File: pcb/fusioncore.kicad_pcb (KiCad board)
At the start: 2 copper layers, 95 x 99 mm, 116 parts, among them J1 Conn_02x12_Top_Bottom, J10 Pump_Misc_1, J11 Pump_Misc_2, J12 Flow_Warm, J13 Flow_Cold, J14 Trigger, J15 Valve_M2, J16 Valve_M3, J17 Valve_M4, J18 Conn_02x03_Top_Bottom, J19 Valve_Air_Lime, J2 Temperature, J20 Valve_Air_Rum, J21 Valve_Air_Out, J22 LED, J23 I2C_DBG, J3 40HAT, J4 Valve_M1, J5 WEIGHT, J6 Pump_Cold, J7 Pump_Warm, J8 Pump_Air, J9 CONN_01X02, Q1 DMG2305UX, Q12 AO3400A, Q13 AO3400A, Q14 AO3400A, Q16 MMBT4403, Q2 DMMT5401, Q3 AO3400A, Q4 AO3400A, Q5 AO3400A, Q6 AO3400A, Q7 AO3400A, SW1 POWER_ON, U1 HX711, U2 CAT24C32, U3 LTC2990, U4 LTC2990, U5 TXB0108DQSR

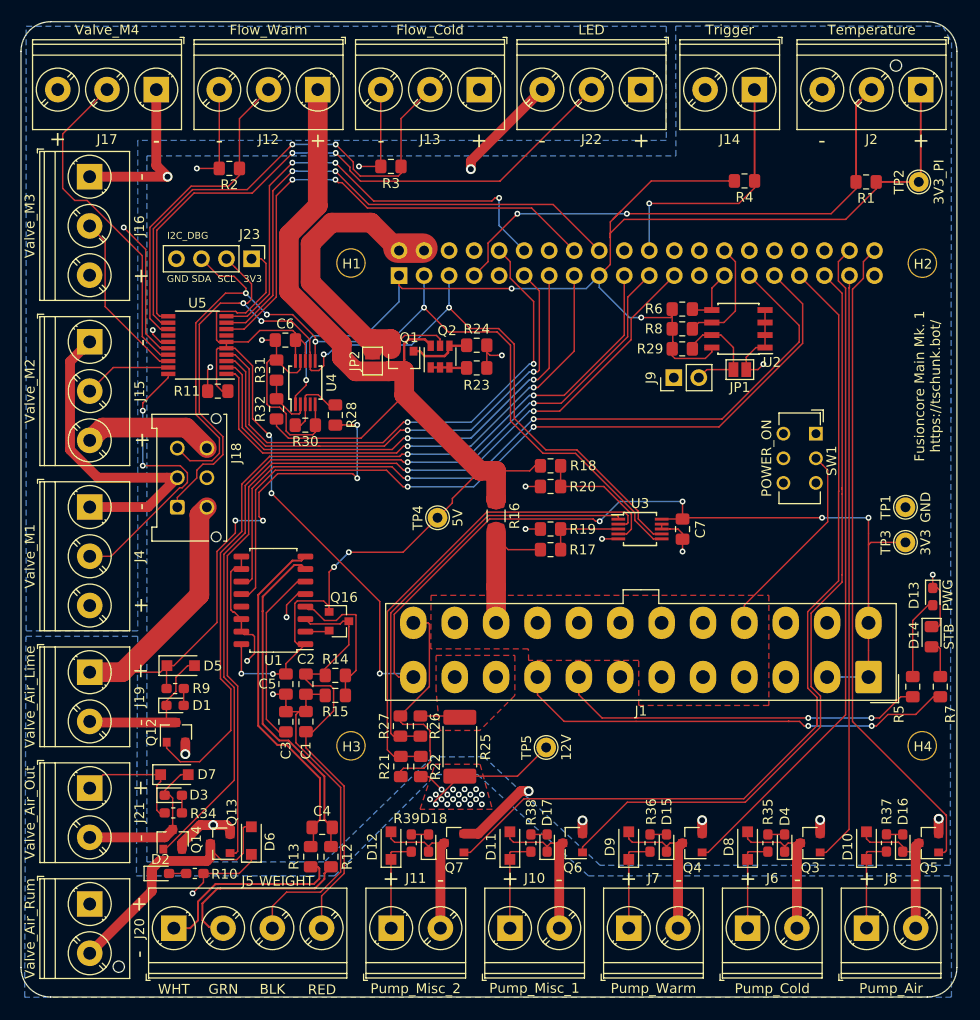
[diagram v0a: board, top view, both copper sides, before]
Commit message: Replaced LTC2990 with INA226 on pcb layout as well
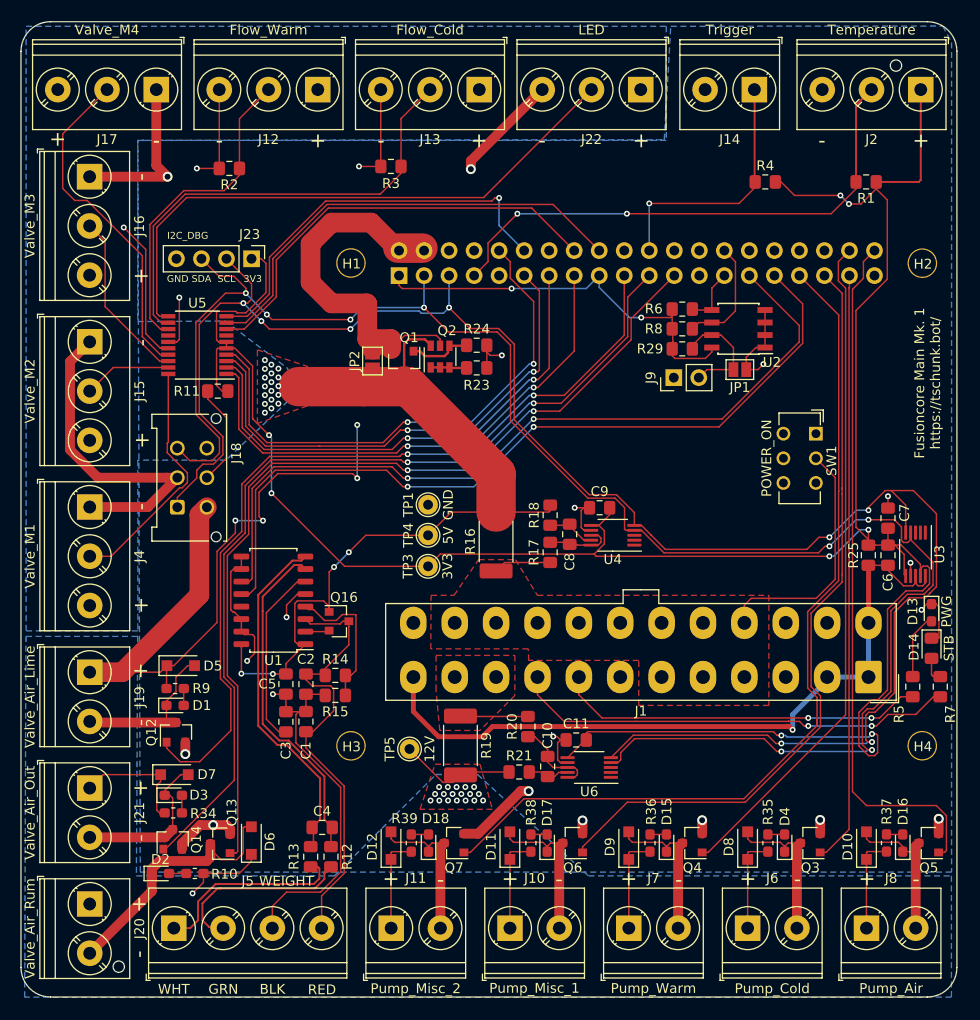
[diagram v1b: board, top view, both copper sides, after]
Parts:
- removed R22, R26, R28, R32: 100K, Resistor_SMD:R_0805_2012Metric_Pad1.15x1.40mm_HandSolder
- removed R27, R30: 20K, Resistor_SMD:R_0805_2012Metric_Pad1.15x1.40mm_HandSolder
- removed R31: 47K, Resistor_SMD:R_0805_2012Metric_Pad1.15x1.40mm_HandSolder
- removed TP2: 3V3_PI, TestPoint:TestPoint_THTPad_D2.0mm_Drill1.0mm
- added C10: 0.1μF, Capacitor_SMD:C_0805_2012Metric_Pad1.15x1.40mm_HandSolder, F.Cu at (102.0, 115.4)
- added C11: 0.1μF, Capacitor_SMD:C_0805_2012Metric_Pad1.15x1.40mm_HandSolder, F.Cu at (104.9, 112.7)
- added C8: 0.1μF, Capacitor_SMD:C_0805_2012Metric_Pad1.15x1.40mm_HandSolder, F.Cu at (104.2, 91.8)
- added C9: 0.1μF, Capacitor_SMD:C_0805_2012Metric_Pad1.15x1.40mm_HandSolder, F.Cu at (107.3, 89.2)
- added U6: INA226, Package_SO:VSSOP-10_3x3mm_P0.5mm, F.Cu at (106.2, 115.5)
- R16: value 0.15 -> 0.008; footprint Resistor_SMD:R_1206_3216Metric_Pad1.42x1.75mm_HandSolder -> Resistor_SMD:R_2512_6332Metric_Pad1.52x3.35mm_HandSolder
- R17, R18: value 100K -> 10
- R19: value 47K -> 0.008; footprint Resistor_SMD:R_0805_2012Metric_Pad1.15x1.40mm_HandSolder -> Resistor_SMD:R_2512_6332Metric_Pad1.52x3.35mm_HandSolder
- R20: value 47K -> 10
- R21: value 20K -> 10
- R25: footprint Resistor_SMD:R_2512_6332Metric_Pad1.52x3.35mm_HandSolder -> Resistor_SMD:R_0805_2012Metric_Pad1.15x1.40mm_HandSolder
- U3, U4: value LTC2990 -> INA226; footprint Package_SO:MSOP-10_3x3mm_P0.5mm -> Package_SO:VSSOP-10_3x3mm_P0.5mm
- moved C6 64.9 mm to (136.6, 94.0), turned to 270 degrees
- moved TP3 48.5 mm to (89.9, 95.1), turned to 270 degrees
- moved TP1 48.5 mm to (89.9, 88.8)
- moved R25 45.8 mm to (134.6, 94.0), turned to 90 degrees
- moved U4 34.8 mm to (108.6, 91.9), turned to 180 degrees
- moved U3 28.1 mm to (139.3, 93.9), turned to 270 degrees
- moved R20 24.5 mm to (100.0, 111.4), turned to 270 degrees
- moved R19 23.8 mm to (93.2, 113.3), turned to 270 degrees
- moved C7 20.9 mm to (136.6, 90.2), turned to 270 degrees
- moved TP5 13.9 mm to (88.0, 113.6)
- moved R21 12.0 mm to (99.1, 116.0), turned to 0 degrees
- moved R18 5.01 mm to (102.3, 89.9), turned to 270 degrees
- moved R16 2.60 mm to (96.8, 92.6)
- moved R4 2.11 mm to (124.1, 56.1), turned to 0 degrees
- moved TP4 2.02 mm to (89.9, 91.9)
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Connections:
- C6 pad 1: GND -> /3V3
- C6 pad 2: /3V3 -> /3V3_ATX
- J1 pad 1: /3V3 -> /3V3_ATX
- J1 pad 12: /3V3 -> /3V3_ATX
- J1 pad 13: /3V3 -> /3V3_ATX
- J1 pad 2: /3V3 -> /3V3_ATX
- J2 pad 1: /3V3_PI -> /3V3
- R1 pad 1: /3V3_PI -> /3V3
- R17 pad 1: Net-(R17-Pad1) -> /5V_ATX
- R17 pad 2: /5V_ATX -> Net-(C8-Pad2)
- R18 pad 1: Net-(R18-Pad1) -> /5V
- R18 pad 2: /5V -> Net-(C8-Pad1)
- R19 pad 1: Net-(R17-Pad1) -> /12V_ATX
- R19 pad 2: GND -> /12V
- R20 pad 1: GND -> /12V_ATX
- R20 pad 2: Net-(R18-Pad1) -> Net-(C10-Pad2)
- R21 pad 1: GND -> /12V
- R21 pad 2: Net-(R21-Pad2) -> Net-(C10-Pad1)
- R25 pad 1: /12V_ATX -> /3V3_ATX
- R25 pad 2: /12V -> /3V3
- R4 pad 2: /3V3_PI -> /3V3
- U3 pad 1: Net-(R26-Pad1) -> (no net)
- U3 pad 10: /3V3 -> /3V3_ATX
- U3 pad 2: Net-(R21-Pad2) -> (no net)
- U3 pad 3: Net-(R17-Pad1) -> (no net)
- U3 pad 4: Net-(R18-Pad1) -> /I2C_SDA
- U3 pad 5: GND -> /I2C_SCL
- U3 pad 6: /I2C_SDA -> /3V3
- U3 pad 7: /I2C_SCL -> GND
- U3 pad 8: GND -> /3V3_ATX
- U3 pad 9: GND -> /3V3
- U4 pad 1: /3V3_PI -> (no net)
- U4 pad 10: /3V3 -> Net-(C8-Pad2)
- U4 pad 2: Net-(R31-Pad2) -> (no net)
- U4 pad 3: Net-(R28-Pad2) -> (no net)
- U4 pad 4: (no net) -> /I2C_SDA
- U4 pad 5: GND -> /I2C_SCL
- U4 pad 6: /I2C_SDA -> /3V3
- U4 pad 7: /I2C_SCL -> GND
- U4 pad 8: /3V3 -> Net-(C8-Pad2)
- U4 pad 9: GND -> Net-(C8-Pad1)
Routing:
- net /I2C_SCL: track 101.6 -> 189.2 mm, vias 4 -> 8
- net /3V3_PI: track 129.3 -> 43.6 mm, vias 3 -> 2
- net /3V3: track 167.5 -> 251.9 mm, vias 7 -> 8
- net /I2C_SDA: track 97.8 -> 181.0 mm, vias 4 -> 8
- net /3V3_ATX: track 0.00 -> 75.2 mm, vias 0 -> 1
- net /5V: track 154.9 -> 99.5 mm, vias 5 -> 23
- net Net-(R21-Pad2): track 48.2 -> 0.00 mm
- net Net-(R26-Pad1): track 42.9 -> 0.00 mm
- net GND: track 241.3 -> 208.2 mm, vias 24 -> 22
- net Net-(R18-Pad1): track 13.5 -> 0.00 mm
- net /5V_ATX: track 15.0 -> 5.84 mm
- net Net-(C10-Pad2): track 0.00 -> 8.74 mm
- net Net-(R17-Pad1): track 7.95 -> 0.00 mm
- net /LED_PWM: track 48.7 -> 41.2 mm, vias 3 -> 1
- net Net-(R28-Pad2): track 7.26 -> 0.00 mm
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- added copper zone on F.Cu, net /5V

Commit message: Cleaned up annotations
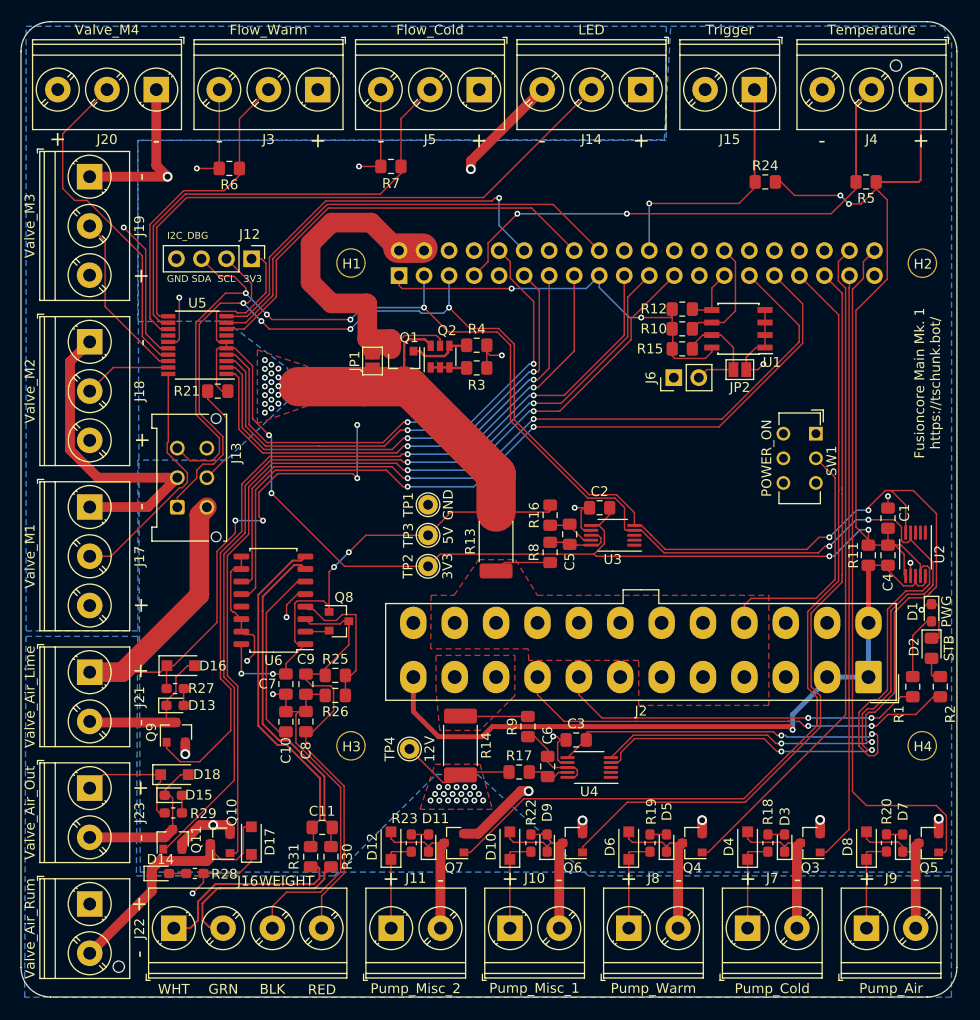
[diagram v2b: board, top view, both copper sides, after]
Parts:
- renumbered C7 to C1, C3 to C10, C4 to C11, C9 to C2, C11 to C3, C6 to C4, C8 to C5, C10 to C6, C5 to C7, C1 to C8, C2 to C9, D13 to D1, D11 to D10, D18 to D11, D1 to D13, D2 to D14, D3 to D15, D5 to D16, D6 to D17, D7 to D18, D14 to D2, D4 to D3, D8 to D4, D15 to D5, D9 to D6, D16 to D7, D10 to D8, D17 to D9, J3 to J1, J23 to J12, J18 to J13, J22 to J14, J14 to J15, J5 to J16, J4 to J17, J15 to J18, J16 to J19, J1 to J2, J17 to J20, J19 to J21, J20 to J22, J21 to J23, J12 to J3, J2 to J4, J13 to J5, J9 to J6, J6 to J7, J7 to J8, J8 to J9, JP2 to JP1, JP1 to JP2, Q13 to Q10, Q14 to Q11, Q16 to Q8, Q12 to Q9, R5 to R1, R8 to R10, R25 to R11, R6 to R12, R16 to R13, R19 to R14, R29 to R15, R18 to R16, R21 to R17, R35 to R18, R36 to R19, R7 to R2, R37 to R20, R11 to R21, R38 to R22, R39 to R23, R4 to R24, R14 to R25, R15 to R26, R9 to R27, R10 to R28, R34 to R29, R23 to R3, R12 to R30, R13 to R31, R24 to R4, R1 to R5, R2 to R6, R3 to R7, R17 to R8, R20 to R9, TP3 to TP2, TP4 to TP3, TP5 to TP4, U2 to U1, U3 to U2, U4 to U3, U6 to U4, U1 to U6

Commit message: Fixed some alignment issues
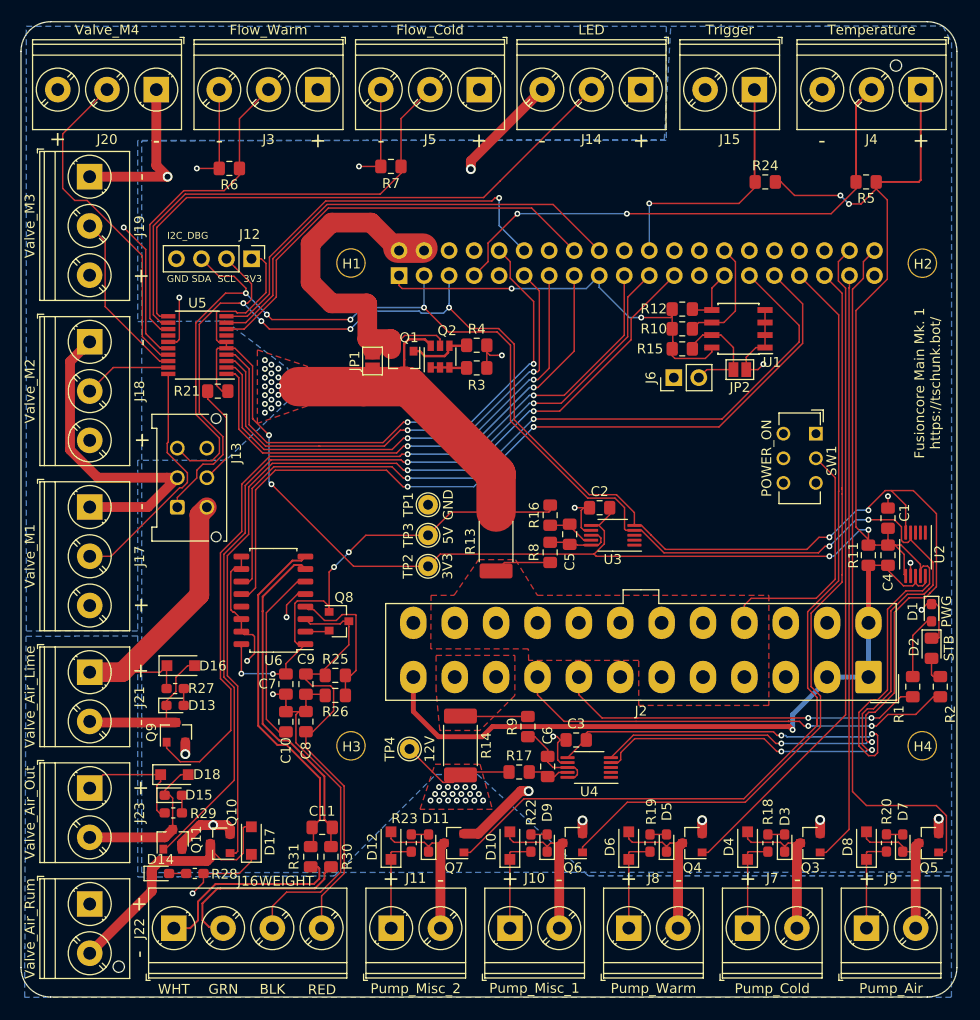
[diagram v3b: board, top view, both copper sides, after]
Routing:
- net /12V: track 157.4 -> 117.1 mm, vias 23 -> 19
- net /3V3: track 251.9 -> 251.4 mm
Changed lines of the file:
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@@
     (thickness 1.6)
     (drawings 95)
-    (tracks 1308)
+    (tracks 1287)
     (zones 0)
     (modules 113)
@@
   (segment (start 73.7235 81.788) (end 73.7235 81.788) (width 0.15) (layer F.Cu) (net 6))
   (via (at 73.7235 81.788) (size 0.6) (drill 0.3) (layers F.Cu B.Cu) (net 6))
-  (segment (start 73.973499 82.037999) (end 73.973499 86.355999) (width 0.15) (layer B.Cu) (net 6))
-  (segment (start 73.7235 81.788) (end 73.973499 82.037999) (width 0.15) (layer B.Cu) (net 6))
-  (via (at 73.973499 87.6808) (size 0.6) (drill 0.3) (layers F.Cu B.Cu) (net 6))
+  (via (at 73.973499 86.7664) (size 0.6) (drill 0.3) (layers F.Cu B.Cu) (net 6))
   (segment (start 88.0175 105.9815) (end 88.374 106.338) (width 0.15) (layer B.Cu) (net 58))
-  (segment (start 73.973499 86.355999) (end 73.973499 87.6808) (width 0.15) (layer B.Cu) (net 6))
   (segment (start 70.2714 72.969) (end 69.3964 72.969) (width 0.15) (layer F.Cu) (net 6))
   (segment (start 72.055499 74.753099) (end 70.2714 72.969) (width 0.15) (layer F.Cu) (net 6))
@@
   (segment (start 86.106 124.847) (end 86.106 131.810668) (width 0.15) (layer F.Cu) (net 8))
   (via (at 65.9638 128.2954) (size 0.6) (drill 0.3) (layers F.Cu B.Cu) (net 8))
-  (via (at 70.3072 90.4494) (size 0.6) (drill 0.3) (layers F.Cu B.Cu) (net 8))
-  (via (at 82.677 86.1568) (size 0.6) (drill 0.3) (layers F.Cu B.Cu) (net 8))
   (segment (start 122.301 124.147) (end 122.301 124.847) (width 0.15) (layer F.Cu) (net 8))
   (segment (start 122.383 124.065) (end 122.301 124.147) (width 0.15) (layer F.Cu) (net 8))
@@
   (segment (start 62.69684 105.84486) (end 63.3603 105.1814) (width 0.15) (layer F.Cu) (net 8))
   (segment (start 55.5244 105.84486) (end 62.69684 105.84486) (width 0.15) (layer F.Cu) (net 8))
-  (segment (start 82.677 80.7466) (end 82.677 80.7466) (width 0.15) (layer F.Cu) (net 8))
-  (via (at 82.677 80.7466) (size 0.6) (drill 0.3) (layers F.Cu B.Cu) (net 8))
-  (segment (start 82.677 81.170864) (end 82.677 86.1568) (width 0.15) (layer B.Cu) (net 8))
-  (segment (start 82.677 80.7466) (end 82.677 81.170864) (width 0.15) (layer B.Cu) (net 8))
-  (segment (start 73.1139 90.4621) (end 73.1266 90.4748) (width 0.15) (layer F.Cu) (net 8))
-  (via (at 73.1139 90.4621) (size 0.6) (drill 0.3) (layers F.Cu B.Cu) (net 8))
-  (segment (start 70.3199 90.4621) (end 70.3072 90.4494) (width 0.15) (layer B.Cu) (net 8))
-  (segment (start 73.1139 90.4621) (end 70.3199 90.4621) (width 0.15) (layer B.Cu) (net 8))
-  (segment (start 64.0603 105.1814) (end 63.3603 105.1814) (width 0.15) (layer F.Cu) (net 8))
-  (segment (start 68.44295 100.79875) (end 64.0603 105.1814) (width 0.15) (layer F.Cu) (net 8))
-  (segment (start 68.44295 93.584586) (end 68.44295 100.79875) (width 0.15) (layer F.Cu) (net 8))
-  (segment (start 70.3072 91.720336) (end 68.44295 93.584586) (width 0.15) (layer F.Cu) (net 8))
-  (segment (start 70.3072 90.4494) (end 70.3072 91.720336) (width 0.15) (layer F.Cu) (net 8))
   (segment (start 67.0687 127.1905) (end 65.9638 128.2954) (width 0.15) (layer F.Cu) (net 8))
   (segment (start 67.0687 126.2761) (end 67.0687 127.1905) (width 0.15) (layer F.Cu) (net 8))
   (segment (start 67.5937 126.2761) (end 67.0687 126.2761) (width 0.15) (layer F.Cu) (net 8))
-  (segment (start 72.70902 90.05722) (end 73.1139 90.4621) (width 0.15) (layer F.Cu) (net 8))
-  (segment (start 72.70902 87.59038) (end 72.70902 90.05722) (width 0.15) (layer F.Cu) (net 8))
-  (segment (start 74.60539 85.69401) (end 72.70902 87.59038) (width 0.15) (layer F.Cu) (net 8))
-  (segment (start 82.677 86.1568) (end 82.21421 85.69401) (width 0.15) (layer F.Cu) (net 8))
-  (segment (start 82.21421 85.69401) (end 74.60539 85.69401) (width 0.15) (layer F.Cu) (net 8))
   (segment (start 70.6927 126.2761) (end 71.9328 125.036) (width 0.15) (layer F.Cu) (net 8))
   (segment (start 71.9328 125.036) (end 71.9328 124.336) (width 0.15) (layer F.Cu) (net 8))
@@
   (segment (start 91.10361 93.85919) (end 89.8652 95.0976) (width 0.15) (layer F.Cu) (net 6))
   (segment (start 106.719202 93.85919) (end 91.10361 93.85919) (width 0.15) (layer F.Cu) (net 6))
-  (segment (start 81.390299 95.0976) (end 89.8652 95.0976) (width 0.15) (layer F.Cu) (net 6))
-  (segment (start 73.973499 87.6808) (end 81.390299 95.0976) (width 0.15) (layer F.Cu) (net 6))
+  (segment (start 73.7235 86.516401) (end 73.973499 86.7664) (width 0.15) (layer B.Cu) (net 6))
+  (segment (start 73.7235 81.788) (end 73.7235 86.516401) (width 0.15) (layer B.Cu) (net 6))
+  (segment (start 82.304699 95.0976) (end 89.8652 95.0976) (width 0.15) (layer F.Cu) (net 6))
+  (segment (start 73.973499 86.7664) (end 82.304699 95.0976) (width 0.15) (layer F.Cu) (net 6))
   (segment (start 92.2207 89.5925) (end 89.8652 91.948) (width 0.15) (layer F.Cu) (net 7))
   (segment (start 96.77146 89.5925) (end 92.2207 89.5925) (width 0.15) (layer F.Cu) (net 7))
@@
     (polygon
       (pts
-        (xy 143.002 41.9227) (xy 143.002 126.1364) (xy 60.6552 126.1364) (xy 60.4012 51.8668) (xy 113.8428 51.8033)
+        (xy 143.002 41.9227) (xy 143.002 126.1364) (xy 60.8076 126.1872) (xy 60.8076 51.9176) (xy 113.8428 51.8033)
         (xy 114.5032 40.2844) (xy 142.113 40.259)
       )
@@
     (polygon
       (pts
-        (xy 60.395303 102.2096) (xy 60.261953 126.5174) (xy 80.366053 126.5174) (xy 90.665753 116.2304) (xy 94.882153 116.2304)
+        (xy 60.4012 102.1588) (xy 60.4012 126.6444) (xy 80.366053 126.5174) (xy 90.665753 116.2304) (xy 94.882153 116.2304)
         (xy 106.145321 126.5174) (xy 142.989753 126.5174) (xy 142.989753 138.8364) (xy 48.920853 138.8364) (xy 49.054203 102.2096)
       )

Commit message: Set I2C Address for INA226s
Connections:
- U2 pad 1: (no net) -> /3V3
- U2 pad 2: (no net) -> GND
- U3 pad 1: (no net) -> /3V3
- U3 pad 2: (no net) -> /3V3
- U4 pad 1: (no net) -> /3V3
- U4 pad 2: (no net) -> /I2C_SDA
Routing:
- net /3V3: track 251.4 -> 265.2 mm
- net /I2C_SDA: track 181.0 -> 187.2 mm
- net GND: track 208.2 -> 210.1 mm, vias 22 -> 23

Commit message: Fixed some more alignment issues
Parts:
- moved R24 1.32 mm to (124.1, 54.8)
- moved R5 1.32 mm to (134.3, 54.8)
- moved R7 0.25 mm to (86.1, 54.8)
- moved R6 0.05 mm to (69.7, 54.8)
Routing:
- net /3V3: track 265.2 -> 266.8 mm

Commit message: Added license
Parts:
- added REF**: OSHW-Logo_5.7x6mm_SilkScreen, Symbol:OSHW-Logo_5.7x6mm_SilkScreen, F.Cu at (139.8, 56.8)
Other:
- board text added: "CC BY-SA 4.0"
